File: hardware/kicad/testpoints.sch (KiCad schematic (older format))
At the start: 25 parts

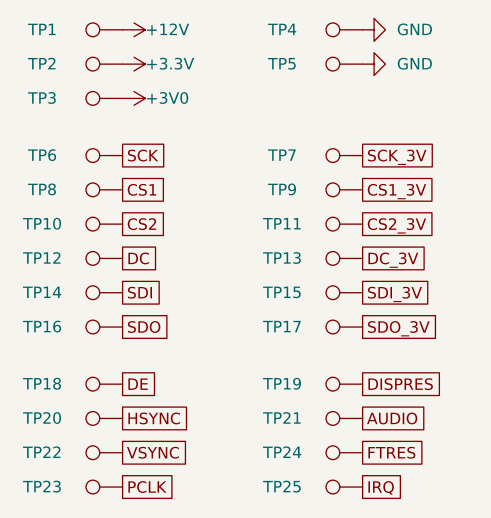
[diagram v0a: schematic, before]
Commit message: Clean up board and expose less debug signals
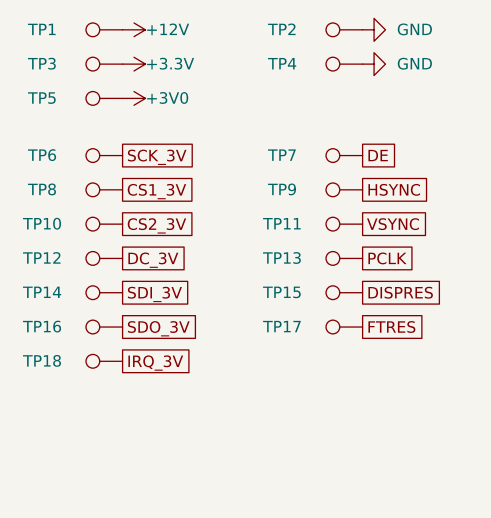
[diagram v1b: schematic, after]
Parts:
- removed TP10, TP12, TP14, TP16, TP21, TP25, TP6, TP8: TestPoint, TestPoint:TestPoint_Pad_D0.5mm, symbol Connector:TestPoint
- added TP18: TestPoint, TestPoint:TestPoint_Pad_D0.5mm, symbol Connector:TestPoint
- renumbered TP11 to TP10, TP22 to TP11, TP13 to TP12, TP23 to TP13, TP15 to TP14, TP19 to TP15, TP17 to TP16, TP24 to TP17, TP4 to TP2, TP2 to TP3, TP5 to TP4, TP3 to TP5, TP7 to TP6, TP18 to TP7, TP9 to TP8, TP20 to TP9
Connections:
- new net IRQ_3V: TP18.1
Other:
- moved on the sheet: TP10, TP11, TP12, TP13, TP14, TP15, TP16, TP17, TP6, TP7, TP8, TP9
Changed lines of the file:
@@
 $EndComp
 $Comp
-L power:+12V #PWR067
+L power:+12V #PWR068
 U 1 1 5F0317D1
 P 5250 2650
-F 0 "#PWR067" H 5250 2500 50  0001 C CNN
+F 0 "#PWR068" H 5250 2500 50  0001 C CNN
 F 1 "+12V" V 5250 2750 50  0000 L CNN
 F 2 "" H 5250 2650 50  0001 C CNN
@@
 $EndComp
 $Comp
-L Connector:TestPoint TP2
+L Connector:TestPoint TP3
 U 1 1 5F0327EC
 P 5250 2800
-F 0 "TP2" V 5250 3150 50  0000 C CNN
+F 0 "TP3" V 5250 3150 50  0000 C CNN
 F 1 "TestPoint" V 5354 2872 50  0001 C CNN
 F 2 "TestPoint:TestPoint_Pad_D0.5mm" H 5450 2800 50  0001 C CNN
@@
 $EndComp
 $Comp
-L power:+3.3V #PWR068
+L power:+3.3V #PWR070
 U 1 1 5F032C4C
 P 5250 2800
-F 0 "#PWR068" H 5250 2650 50  0001 C CNN
+F 0 "#PWR070" H 5250 2650 50  0001 C CNN
 F 1 "+3.3V" V 5250 2900 50  0000 L CNN
 F 2 "" H 5250 2800 50  0001 C CNN
@@
 $EndComp
 $Comp
-L Connector:TestPoint TP3
+L Connector:TestPoint TP5
 U 1 1 5F03331D
 P 5250 2950
-F 0 "TP3" V 5250 3300 50  0000 C CNN
+F 0 "TP5" V 5250 3300 50  0000 C CNN
 F 1 "TestPoint" V 5354 3022 50  0001 C CNN
 F 2 "TestPoint:TestPoint_Pad_D0.5mm" H 5450 2950 50  0001 C CNN
@@
 $EndComp
 $Comp
-L power:+3V0 #PWR069
+L power:+3V0 #PWR072
 U 1 1 5F033611
 P 5250 2950
-F 0 "#PWR069" H 5250 2800 50  0001 C CNN
+F 0 "#PWR072" H 5250 2800 50  0001 C CNN
 F 1 "+3V0" V 5250 3050 50  0000 L CNN
 F 2 "" H 5250 2950 50  0001 C CNN
@@
 $EndComp
 $Comp
-L Connector:TestPoint TP4
+L Connector:TestPoint TP2
 U 1 1 5F035E62
 P 6300 2650
-F 0 "TP4" V 6300 3000 50  0000 C CNN
+F 0 "TP2" V 6300 3000 50  0000 C CNN
 F 1 "TestPoint" V 6404 2722 50  0001 C CNN
 F 2 "TestPoint:TestPoint_Pad_1.0x1.0mm" H 6500 2650 50  0001 C CNN
@@
 $EndComp
 $Comp
-L power:GND #PWR070
+L power:GND #PWR069
 U 1 1 5F0362A5
 P 6300 2650
-F 0 "#PWR070" H 6300 2400 50  0001 C CNN
+F 0 "#PWR069" H 6300 2400 50  0001 C CNN
 F 1 "GND" V 6300 2500 50  0000 R CNN
 F 2 "" H 6300 2650 50  0001 C CNN
@@
 $EndComp
 $Comp
-L Connector:TestPoint TP5
+L Connector:TestPoint TP4
 U 1 1 5F0363CB
 P 6300 2800
-F 0 "TP5" V 6300 3150 50  0000 C CNN
+F 0 "TP4" V 6300 3150 50  0000 C CNN
 F 1 "TestPoint" V 6404 2872 50  0001 C CNN
 F 2 "TestPoint:TestPoint_Pad_1.0x1.0mm" H 6500 2800 50  0001 C CNN
@@
 $Comp
 L Connector:TestPoint TP6
-U 1 1 5F036C77
+U 1 1 5F042349
 P 5250 3200
 F 0 "TP6" V 5250 3550 50  0000 C CNN
@@
 $EndComp
 Text GLabel 5250 3200 2    50   UnSpc ~ 0
-SCK
+SCK_3V
 $Comp
 L Connector:TestPoint TP8
-U 1 1 5F037409
+U 1 1 5F042350
 P 5250 3350
 F 0 "TP8" V 5250 3700 50  0000 C CNN
@@
 $EndComp
 Text GLabel 5250 3350 2    50   UnSpc ~ 0
-CS1
+CS1_3V
 $Comp
 L Connector:TestPoint TP10
-U 1 1 5F037703
+U 1 1 5F042357
 P 5250 3500
 F 0 "TP10" V 5250 3850 50  0000 C CNN
@@
 $EndComp
 Text GLabel 5250 3500 2    50   UnSpc ~ 0
-CS2
+CS2_3V
 $Comp
 L Connector:TestPoint TP12
-U 1 1 5F037A44
+U 1 1 5F04235E
 P 5250 3650
 F 0 "TP12" V 5250 4000 50  0000 C CNN
@@
 $EndComp
 Text GLabel 5250 3650 2    50   UnSpc ~ 0
-DC
+DC_3V
 $Comp
 L Connector:TestPoint TP14
-U 1 1 5F037E05
+U 1 1 5F042365
 P 5250 3800
 F 0 "TP14" V 5250 4150 50  0000 C CNN
@@
 $EndComp
 Text GLabel 5250 3800 2    50   UnSpc ~ 0
-SDI
+SDI_3V
 $Comp
 L Connector:TestPoint TP16
-U 1 1 5F03819B
+U 1 1 5F04236C
 P 5250 3950
 F 0 "TP16" V 5250 4300 50  0000 C CNN
@@
 $EndComp
 Text GLabel 5250 3950 2    50   UnSpc ~ 0
-SDO
+SDO_3V
 $Comp
 L Connector:TestPoint TP7
-U 1 1 5F042349
+U 1 1 5F04BDAF
 P 6300 3200
 F 0 "TP7" V 6300 3550 50  0000 C CNN
@@
 $EndComp
 Text GLabel 6300 3200 2    50   UnSpc ~ 0
-SCK_3V
+DE
 $Comp
 L Connector:TestPoint TP9
-U 1 1 5F042350
+U 1 1 5F04C63C
 P 6300 3350
 F 0 "TP9" V 6300 3700 50  0000 C CNN
@@
 $EndComp
 Text GLabel 6300 3350 2    50   UnSpc ~ 0
-CS1_3V
+HSYNC
 $Comp
 L Connector:TestPoint TP11
-U 1 1 5F042357
+U 1 1 5F04CB5A
 P 6300 3500
 F 0 "TP11" V 6300 3850 50  0000 C CNN
@@
 $EndComp
 Text GLabel 6300 3500 2    50   UnSpc ~ 0
-CS2_3V
+VSYNC
 $Comp
 L Connector:TestPoint TP13
-U 1 1 5F04235E
+U 1 1 5F04CF0A
 P 6300 3650
 F 0 "TP13" V 6300 4000 50  0000 C CNN
@@
 $EndComp
 Text GLabel 6300 3650 2    50   UnSpc ~ 0
-DC_3V
+PCLK
 $Comp
 L Connector:TestPoint TP15
-U 1 1 5F042365
+U 1 1 5F04D431
 P 6300 3800
 F 0 "TP15" V 6300 4150 50  0000 C CNN
@@
 $EndComp
 Text GLabel 6300 3800 2    50   UnSpc ~ 0
-SDI_3V
+DISPRES
 $Comp
 L Connector:TestPoint TP17
-U 1 1 5F04236C
+U 1 1 5F0486C1
 P 6300 3950
 F 0 "TP17" V 6300 4300 50  0000 C CNN
@@
 $EndComp
 Text GLabel 6300 3950 2    50   UnSpc ~ 0
-SDO_3V
+FTRES
 $Comp
 L Connector:TestPoint TP18
-U 1 1 5F04BDAF
-P 5250 4200
-F 0 "TP18" V 5250 4550 50  0000 C CNN
-F 1 "TestPoint" V 5354 4272 50  0001 C CNN
-F 2 "TestPoint:TestPoint_Pad_D0.5mm" H 5450 4200 50  0001 C CNN
-F 3 "~" H 5450 4200 50  0001 C CNN
-	1    5250 4200
-	0    -1   -1   0
-$EndComp
-Text GLabel 5250 4200 2    50   UnSpc ~ 0
-DE
-$Comp
-L Connector:TestPoint TP20
-U 1 1 5F04C63C
-P 5250 4350
-F 0 "TP20" V 5250 4700 50  0000 C CNN
-F 1 "TestPoint" V 5354 4422 50  0001 C CNN
-F 2 "TestPoint:TestPoint_Pad_D0.5mm" H 5450 4350 50  0001 C CNN
-F 3 "~" H 5450 4350 50  0001 C CNN
-	1    5250 4350
-	0    -1   -1   0
-$EndComp
-Text GLabel 5250 4350 2    50   UnSpc ~ 0
-HSYNC
-$Comp
-L Connector:TestPoint TP22
-U 1 1 5F04CB5A
-P 5250 4500
-F 0 "TP22" V 5250 4850 50  0000 C CNN
-F 1 "TestPoint" V 5354 4572 50  0001 C CNN
-F 2 "TestPoint:TestPoint_Pad_D0.5mm" H 5450 4500 50  0001 C CNN
-F 3 "~" H 5450 4500 50  0001 C CNN
-	1    5250 4500
-	0    -1   -1   0
-$EndComp
-Text GLabel 5250 4500 2    50   UnSpc ~ 0
-VSYNC
-$Comp
-L Connector:TestPoint TP23
-U 1 1 5F04CF0A
-P 5250 4650
-F 0 "TP23" V 5250 5000 50  0000 C CNN
-F 1 "TestPoint" V 5354 4722 50  0001 C CNN
-F 2 "TestPoint:TestPoint_Pad_D0.5mm" H 5450 4650 50  0001 C CNN
-F 3 "~" H 5450 4650 50  0001 C CNN
-	1    5250 4650
-	0    -1   -1   0
-$EndComp
-Text GLabel 5250 4650 2    50   UnSpc ~ 0
-PCLK
-$Comp
-L Connector:TestPoint TP19
-U 1 1 5F04D431
-P 6300 4200
-F 0 "TP19" V 6300 4550 50  0000 C CNN
-F 1 "TestPoint" V 6404 4272 50  0001 C CNN
-F 2 "TestPoint:TestPoint_Pad_D0.5mm" H 6500 4200 50  0001 C CNN
-F 3 "~" H 6500 4200 50  0001 C CNN
-	1    6300 4200
-	0    -1   -1   0
-$EndComp
-Text GLabel 6300 4200 2    50   UnSpc ~ 0
-DISPRES
-$Comp
-L Connector:TestPoint TP21
-U 1 1 5F04DCE3
-P 6300 4350
-F 0 "TP21" V 6300 4700 50  0000 C CNN
-F 1 "TestPoint" V 6404 4422 50  0001 C CNN
-F 2 "TestPoint:TestPoint_Pad_D0.5mm" H 6500 4350 50  0001 C CNN
-F 3 "~" H 6500 4350 50  0001 C CNN
-	1    6300 4350
-	0    -1   -1   0
-$EndComp
-Text GLabel 6300 4350 2    50   UnSpc ~ 0
-AUDIO
-$Comp
-L Connector:TestPoint TP24
-U 1 1 5F0486C1
-P 6300 4500
-F 0 "TP24" V 6300 4850 50  0000 C CNN
-F 1 "TestPoint" V 6404 4572 50  0001 C CNN
-F 2 "TestPoint:TestPoint_Pad_D0.5mm" H 6500 4500 50  0001 C CNN
-F 3 "~" H 6500 4500 50  0001 C CNN
-	1    6300 4500
-	0    -1   -1   0
-$EndComp
-Text GLabel 6300 4500 2    50   UnSpc ~ 0
-FTRES
-$Comp
-L Connector:TestPoint TP25
-U 1 1 5F048FDB
-P 6300 4650
-F 0 "TP25" V 6300 5000 50  0000 C CNN
-F 1 "TestPoint" V 6404 4722 50  0001 C CNN
-F 2 "TestPoint:TestPoint_Pad_D0.5mm" H 6500 4650 50  0001 C CNN
-F 3 "~" H 6500 4650 50  0001 C CNN
-	1    6300 4650
-	0    -1   -1   0
-$EndComp
-Text GLabel 6300 4650 2    50   UnSpc ~ 0
-IRQ
+U 1 1 5F15817D
+P 5250 4100
+F 0 "TP18" V 5250 4450 50  0000 C CNN
+F 1 "TestPoint" V 5354 4172 50  0001 C CNN
+F 2 "TestPoint:TestPoint_Pad_D0.5mm" H 5450 4100 50  0001 C CNN
+F 3 "~" H 5450 4100 50  0001 C CNN
+	1    5250 4100
+	0    -1   -1   0
+$EndComp
+Text GLabel 5250 4100 2    50   UnSpc ~ 0
+IRQ_3V
 $EndSCHEMATC
